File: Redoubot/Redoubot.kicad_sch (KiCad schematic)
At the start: 33 parts, among them J1 Connecteur batterie, J2 Moteur 1, J3 Moteur 2, J4 TOF, J5 MPU-6050, J6 ADA3595, U1 STM32G431RBTx, U2 DRV8833PWP, U3 BQ25896RTWR

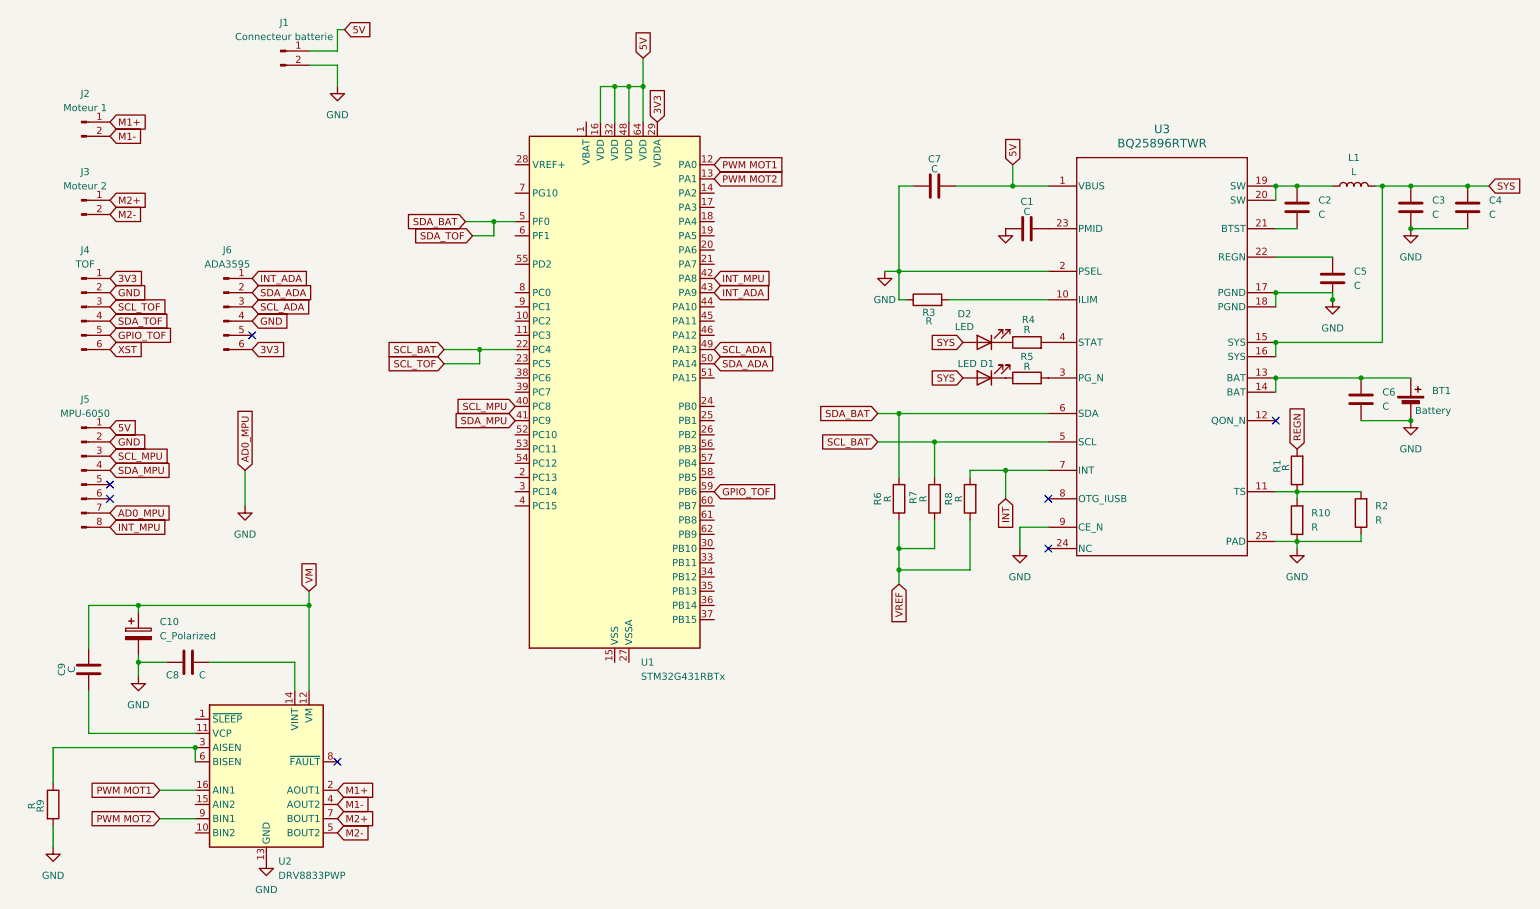
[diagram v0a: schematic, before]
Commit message: chore: add .ioc v0.1; removed nested kicad files; fixed kicad libraries not registering
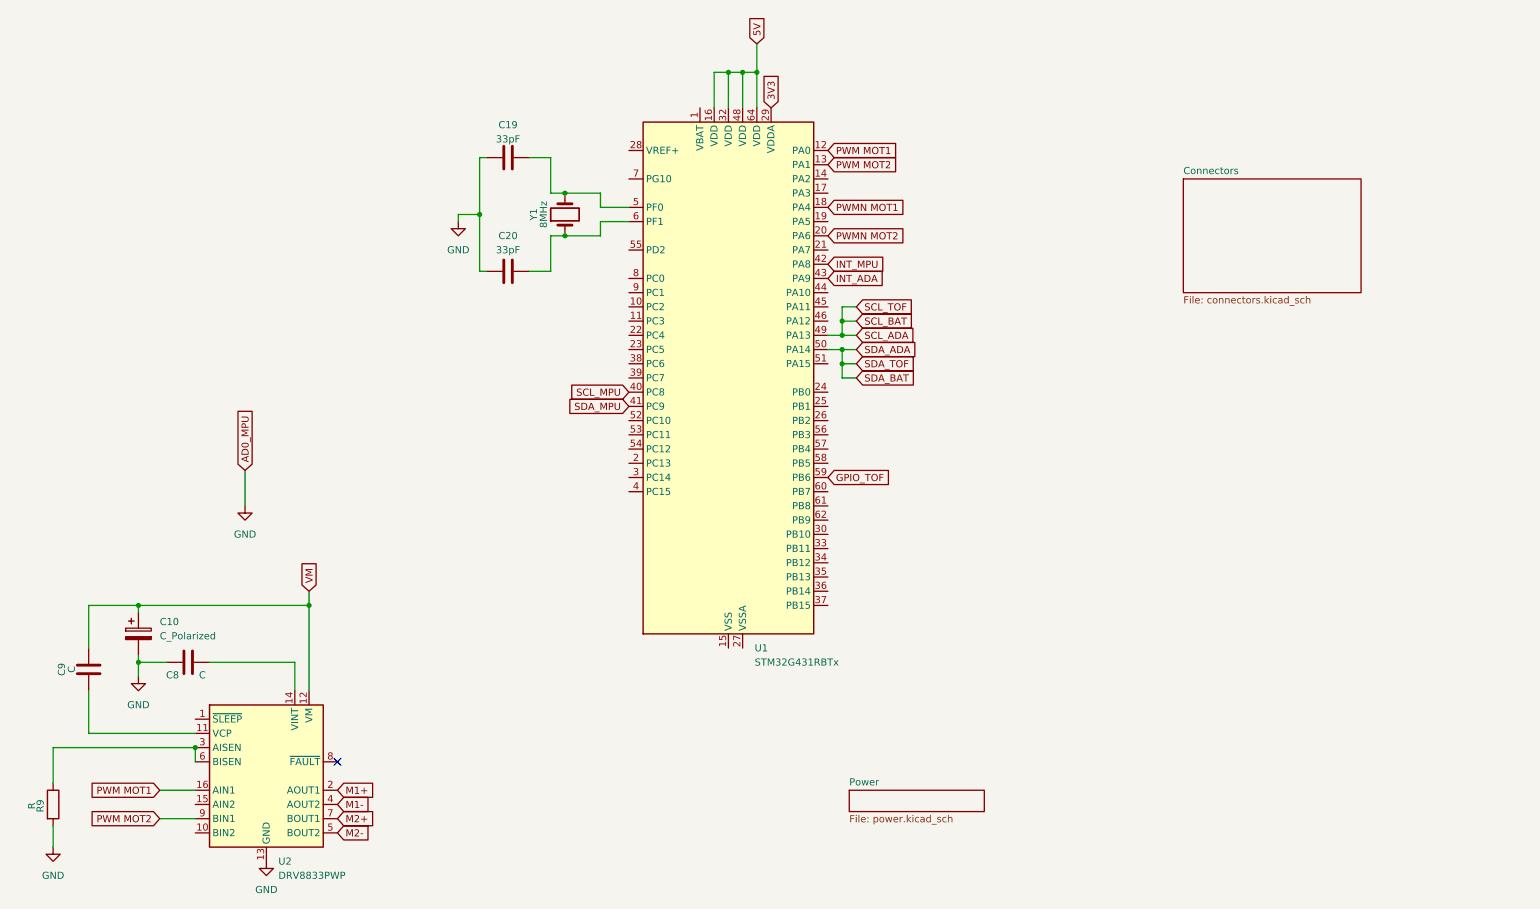
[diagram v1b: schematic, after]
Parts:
- removed BT1: Battery, symbol Device:Battery_Cell
- removed C1, C2, C3, C4, C5, C6, C7: C, symbol Device:C
- removed D1, D2: LED, symbol Device:LED
- removed J1: Connecteur batterie, symbol Connector:Conn_01x02_Pin
- removed J2: Moteur 1, symbol Connector:Conn_01x02_Pin
- removed J3: Moteur 2, symbol Connector:Conn_01x02_Pin
- removed J4: TOF, symbol Connector:Conn_01x06_Pin
- removed J5: MPU-6050, symbol Connector:Conn_01x08_Pin
- removed J6: ADA3595, symbol Connector:Conn_01x06_Pin
- removed L1: L, symbol Device:L
- removed R1, R10, R2, R3, R4, R5, R6, R7, R8: R, symbol Device:R
- removed U3: BQ25896RTWR, RTW0024H, symbol BQ25896RTWR:BQ25896RTWR
- added C19, C20: 33pF, symbol Device:C
- added Y1: 8MHz, symbol Device:Crystal
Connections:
- net GND: now also C19.1, C20.1
- net PWMN MOT1: now reaches U1.18 (PA4)
- net PWMN MOT2: now reaches U1.20 (PA6)
- net at U1.6 (PF1): now also C20.2, Y1.1
- net SCL_BAT: no longer names the net of U1.22 (PC4)
- net SDA_BAT: no longer names the net of U1.5 (PF0)
- net SDA_BAT: now also C19.2, Y1.2
- no-connect marks 7 -> 1
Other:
- added sheet Connectors (connectors.kicad_sch)
- added sheet Power (power.kicad_sch)

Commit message: chore: renaming of hierchical sheet power to power_management to better match the use, creation of drivers and sensors HS to have clear sheets
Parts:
- removed C10: C_Polarized, symbol Device:C_Polarized
- removed C8, C9: C, symbol Device:C
- removed R9: R, symbol Device:R
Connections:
- net PWM MOT1: no longer U2.16 (AIN1)
- net PWM MOT2: no longer U2.9 (BIN1)
- net at U2.3 (AISEN): no longer U2.6 (BISEN)
- net M1+: no longer names the net of U2.2 (AOUT1)
- net M1-: no longer names the net of U2.4 (AOUT2)
- net M2+: no longer names the net of U2.7 (BOUT1)
- net M2-: no longer names the net of U2.5 (BOUT2)
- net VM: no longer names the net of U2.12 (VM)
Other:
- sheet Power renamed Power_management
- added sheet Drivers (drivers.kicad_sch)
- added sheet Sensors (sensors.kicad_sch)
- sheet Power_management: file power.kicad_sch -> power_management.kicad_sch

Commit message: feat: motor driver wired in parallel mode
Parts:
- removed U2: DRV8833PWP, Package_SO:HTSSOP-16-1EP_4.4x5mm_P0.65mm_EP3.4x5mm_Mask2.46x2.31mm_ThermalVias, symbol Driver_Motor:DRV8833PWP
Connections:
- no-connect marks 1 -> 0
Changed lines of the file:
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@@
 		(color 0 0 0 0)
-	)
-	(no_connect
-		(at 71.12 148.59)
 	)
 	(wire
@@
 	)
 	(symbol
-		(lib_id "power:GND")
-		(at 58.42 166.37 0)
-		(unit 1)
-		(body_style 1)
-		(exclude_from_sim no)
-		(in_bom yes)
-		(on_board yes)
-		(in_pos_files yes)
-		(dnp no)
-		(fields_autoplaced yes)
-		(property "Reference" "#PWR011"
-			(at 58.42 172.72 0)
-			(hide yes)
-			(show_name no)
-			(do_not_autoplace no)
-			(effects
-				(font
-					(size 1.27 1.27)
-				)
-			)
-		)
-		(property "Value" "GND"
-			(at 58.42 171.45 0)
-			(show_name no)
-			(do_not_autoplace no)
-			(effects
-				(font
-					(size 1.27 1.27)
-				)
-			)
-		)
-		(property "Footprint" ""
-			(at 58.42 166.37 0)
-			(hide yes)
-			(show_name no)
-			(do_not_autoplace no)
-			(effects
-				(font
-					(size 1.27 1.27)
-				)
-			)
-		)
-		(property "Datasheet" ""
-			(at 58.42 166.37 0)
-			(hide yes)
-			(show_name no)
-			(do_not_autoplace no)
-			(effects
-				(font
-					(size 1.27 1.27)
-				)
-			)
-		)
-		(property "Description" "Power symbol creates a global label with name \"GND\" , ground"
-			(at 58.42 166.37 0)
-			(hide yes)
-			(show_name no)
-			(do_not_autoplace no)
-			(effects
-				(font
-					(size 1.27 1.27)
-				)
-			)
-		)
-		(pin "1"
-		)
-		(instances
-			(project "Redoubot"
-				(path "/43131b41-4104-4cd6-9c2f-4d5da1687300"
-					(reference "#PWR011")
-					(unit 1)
-				)
-			)
-		)
-	)
-	(symbol
 		(lib_id "Device:C")
 		(at 101.6 40.64 90)
@@
 					(unit 1)
 				)
-			)
-		)
-	)
-	(symbol
-		(lib_id "Driver_Motor:DRV8833PWP")
-		(at 58.42 151.13 0)
-		(unit 1)
-		(body_style 1)
-		(exclude_from_sim no)
-		(in_bom yes)
-		(on_board yes)
-		(in_pos_files yes)
-		(dnp no)
-		(fields_autoplaced yes)
-		(property "Reference" "U2"
-			(at 60.5633 166.37 0)
-			(show_name no)
-			(do_not_autoplace no)
-			(effects
-				(font
-					(size 1.27 1.27)
-				)
-				(justify left)
-			)
-		)
-		(property "Value" "DRV8833PWP"
-			(at 60.5633 168.91 0)
-			(show_name no)
-			(do_not_autoplace no)
-			(effects
-				(font
-					(size 1.27 1.27)
-				)
-				(justify left)
-			)
-		)
-		(property "Footprint" "Package_SO:HTSSOP-16-1EP_4.4x5mm_P0.65mm_EP3.4x5mm_Mask2.46x2.31mm_ThermalVias"
-			(at 63.5 166.37 0)
-			(hide yes)
-			(show_name no)
-			(do_not_autoplace no)
-			(effects
-				(font
-					(size 1.27 1.27)
-				)
-				(justify left)
-			)
-		)
-		(property "Datasheet" "http://www.ti.com/lit/ds/symlink/drv8833.pdf"
-			(at 63.5 168.91 0)
-			(hide yes)
-			(show_name no)
-			(do_not_autoplace no)
-			(effects
-				(font
-					(size 1.27 1.27)
-				)
-				(justify left)
-			)
-		)
-		(property "Description" "Dual H-Bridge Motor Driver, HTSSOP-16"
-			(at 58.42 151.13 0)
-			(hide yes)
-			(show_name no)
-			(do_not_autoplace no)
-			(effects
-				(font
-					(size 1.27 1.27)
-				)
-			)
-		)
-		(pin "1"
-		)
-		(pin "2"
-		)
-		(pin "3"
-		)
-		(pin "4"
-		)
-		(pin "5"
-		)
-		(pin "6"
-		)
-		(pin "7"
-		)
-		(pin "8"
-		)
-		(pin "9"
-		)
-		(pin "10"
-		)
-		(pin "11"
-		)
-		(pin "12"
-		)
-		(pin "13"
-		)
-		(pin "14"
-		)
-		(pin "15"
-		)
-		(pin "16"
-		)
-		(pin "17"
-		)
-		(instances
-			(project "Redoubot"
-				(path "/43131b41-4104-4cd6-9c2f-4d5da1687300"
-					(reference "U2")
-					(unit 1)
-				)

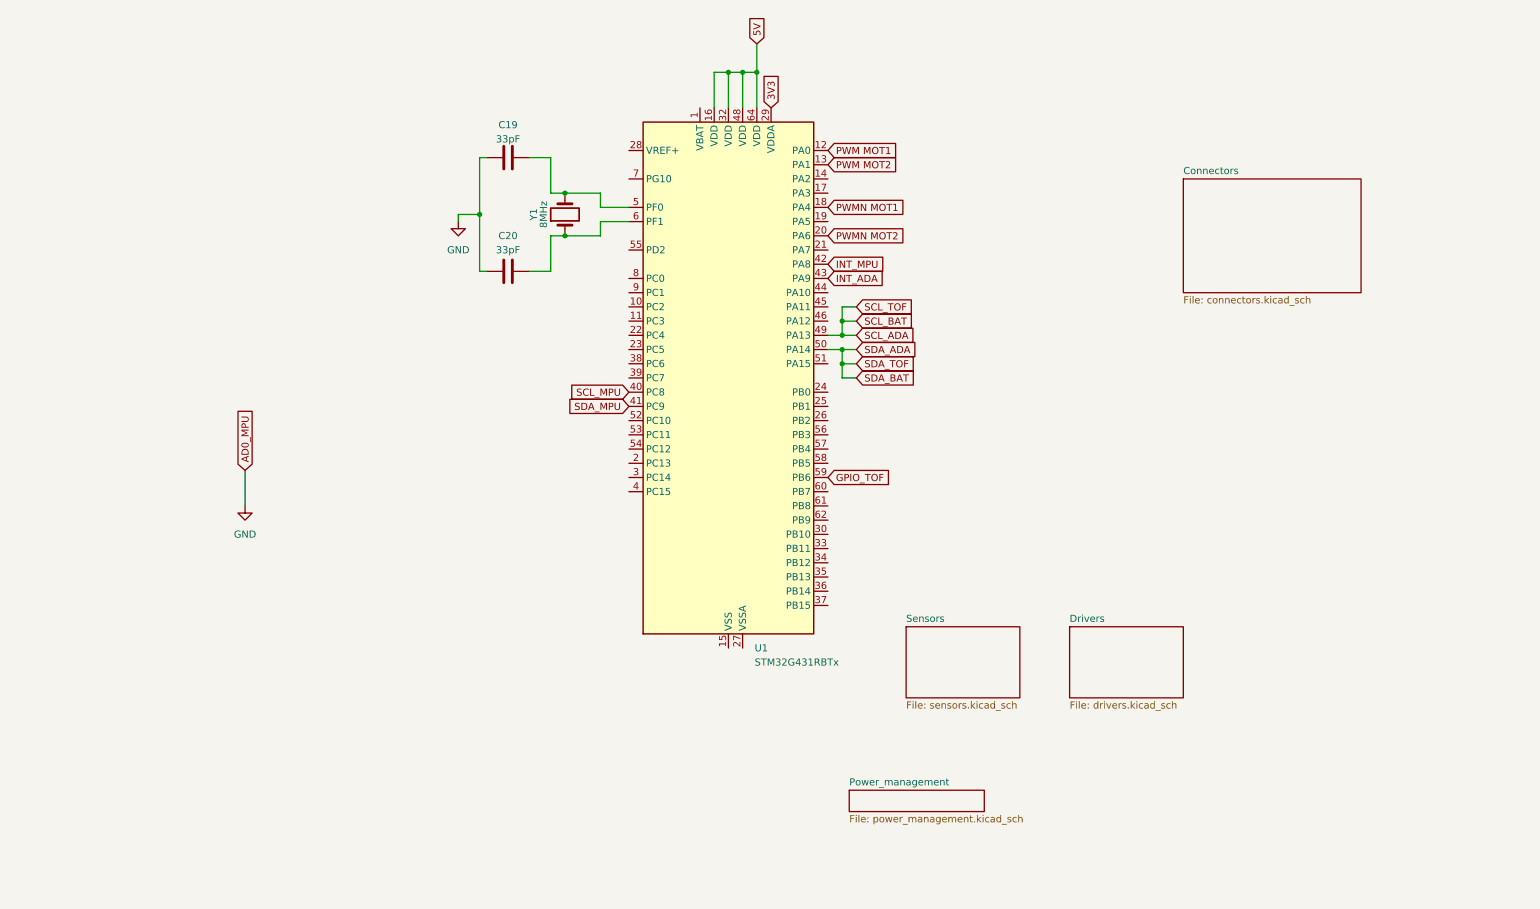
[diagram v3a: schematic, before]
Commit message: feat: added all remaining connectors & finished putting values on components
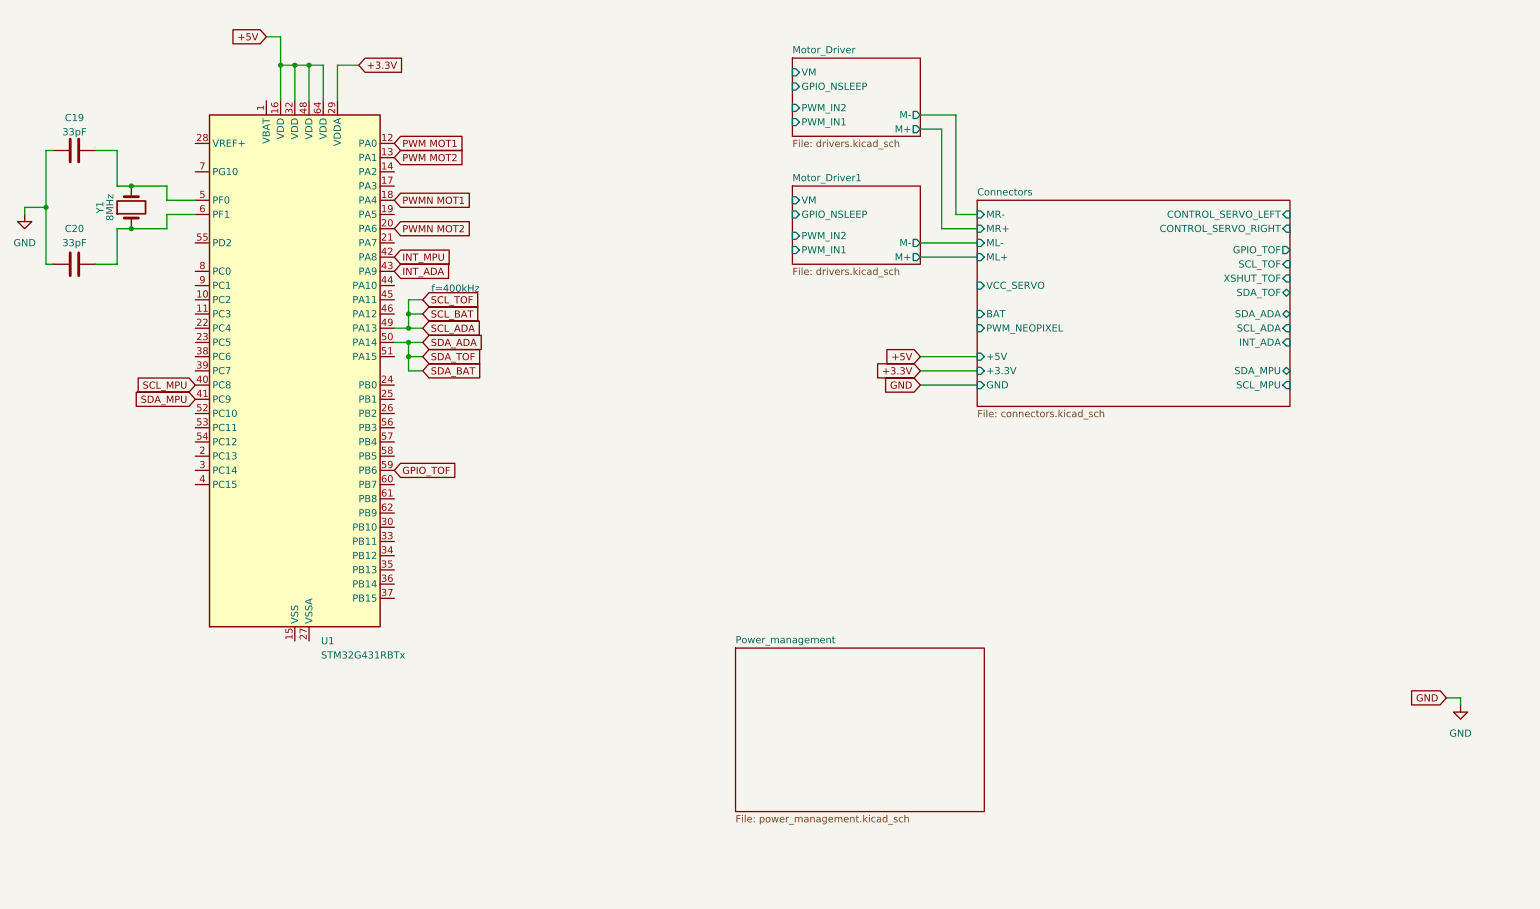
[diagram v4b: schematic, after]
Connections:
- net 3V3 renamed +3.3V
- net 5V renamed +5V
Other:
- sheet Drivers renamed Motor_Driver
- removed sheet Sensors
- added sheet Motor_Driver1 (drivers.kicad_sch)
- sheet Connectors ports: added +3.3V, +5V, BAT, CONTROL_SERVO_LEFT, CONTROL_SERVO_RIGHT, GND, GPIO_TOF, INT_ADA, ML+, ML-, MR+, MR-, PWM_NEOPIXEL, SCL_ADA, SCL_MPU, SCL_TOF, SDA_ADA, SDA_MPU, SDA_TOF, VCC_SERVO, XSHUT_TOF; removed none
- sheet Motor_Driver ports: added GPIO_NSLEEP, M+, M-, PWM_IN1, PWM_IN2, VM; removed none
- note added: "f=400kHz"
- moved on the sheet: C19, C20, U1, Y1

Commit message: chore: wired everything possible atm, wrote down every missing links, waiting for .ioc to continue
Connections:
- net PWM MOT1 renamed PWM_M1
- net PWM MOT2 renamed PWM_M2
- net PWMN MOT1 renamed PWMN_M1
- net PWMN MOT2 renamed PWMN_M2
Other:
- sheet Motor_Driver renamed Motor_Driver_Right
- sheet Motor_Driver1 renamed Motor_Driver_Left
- sheet Power_management ports: added +3.3V, +5V, BAT, GPOUT_FUEL_GAUGE, PWR_INT, SCL_BAT, SDA_BAT, SYS; removed none
- note added: "XSHUT_TOF NOT WIRED INT_ADA NOT WIRED GPIO_OUR_FG NOT WIRED PWR_INT NOT WIRED SYS NOT WIRED PWM_NEOPIXEL NOT WIRED CONTROL_SERVO_RIGHT & LEFT NOT WIRED GPOUT_FUEL_GAUGE NOT WIRED"
